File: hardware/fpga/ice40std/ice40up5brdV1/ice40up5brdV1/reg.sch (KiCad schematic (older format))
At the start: 1 part

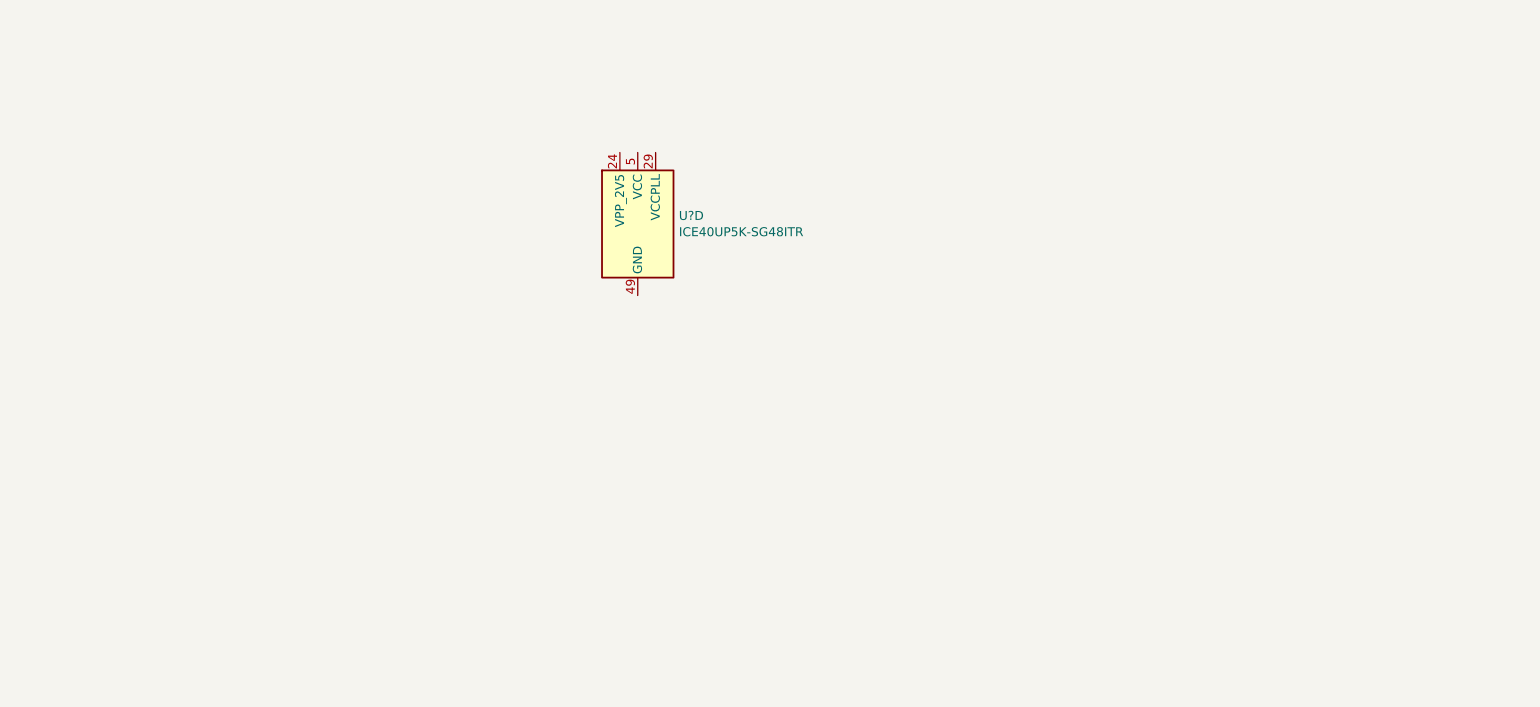
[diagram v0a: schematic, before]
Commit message: usb => mcu => ice40 fpga => NAND flash bridge started
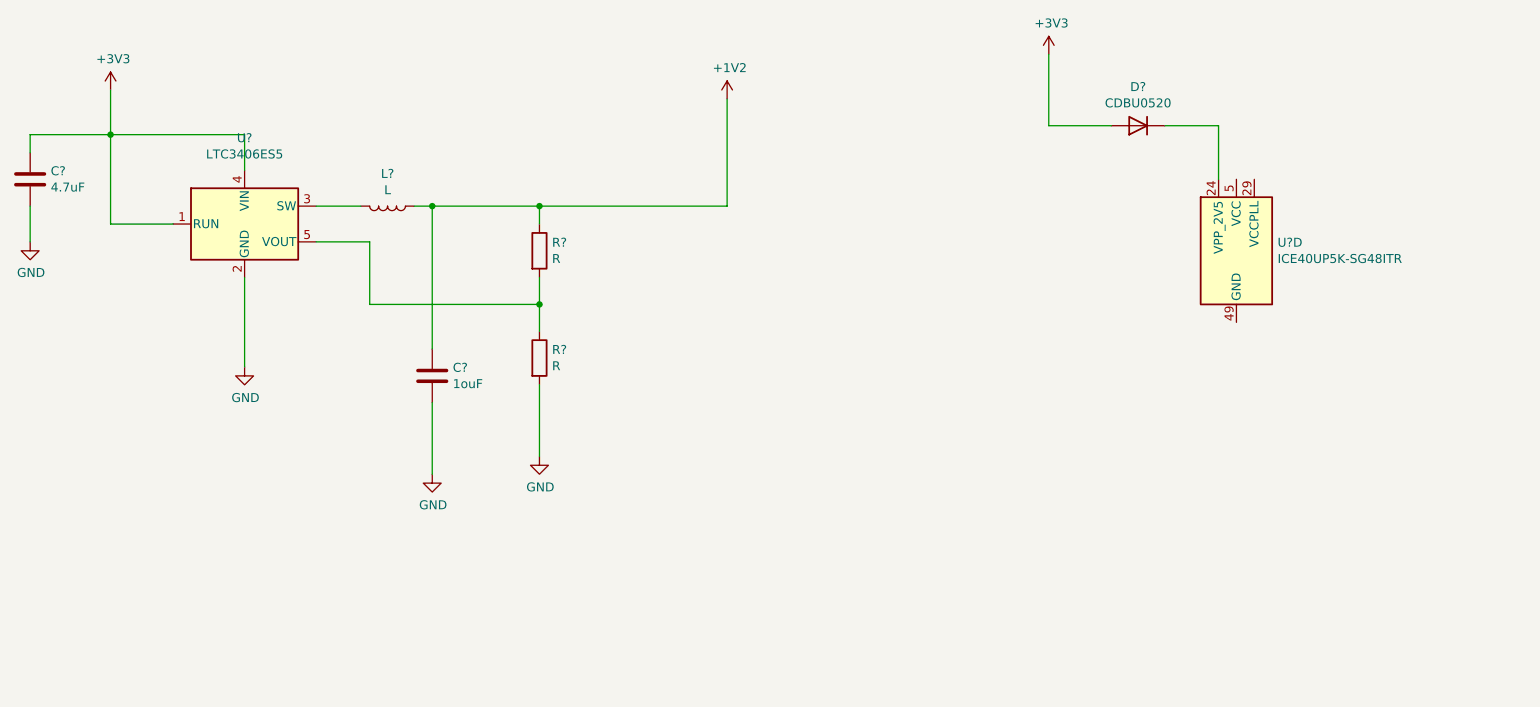
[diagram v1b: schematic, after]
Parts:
- added C?: 4.7uF, Capacitor_SMD:C_0402_1005Metric, symbol Device:C
- added C?: 1ouF, Capacitor_SMD:C_0603_1608Metric, symbol Device:C
- added D?: CDBU0520, Diode_SMD:D_0603_1608Metric, symbol Device:D
- added L?: L, symbol Device:L
- added R? (x2): R, symbol Device:R
- added U?: LTC3406ES5, Package_TO_SOT_SMD:TSOT-23-5, symbol Regulator_Switching:LTC3406ES5
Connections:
- net at U?.24 (VPP_2V5): now also D?.1 (K)
- new net: L?.2, U?.3 (SW)
- new net: R?.1, R?.2, U?.5 (VOUT)
- new net +1V2: C?.1, L?.1, R?.1
- new net +3V3: C?.1, D?.2 (A), U?.1 (RUN), U?.4 (VIN)
- new net GND: C?.2, C?.2, R?.2, U?.2 (GND)
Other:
- moved on the sheet: U?D
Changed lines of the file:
@@
 L FPGA_Lattice:ICE40UP5K-SG48ITR U?
 U 4 1 60A7161F
-P 4500 3100
-F 0 "U?" H 4730 3146 50  0000 L CNN
-F 1 "ICE40UP5K-SG48ITR" H 4730 3055 50  0000 L CNN
-F 2 "Package_DFN_QFN:QFN-48-1EP_7x7mm_P0.5mm_EP5.6x5.6mm" H 4500 1750 50  0001 C CNN
-F 3 "http://www.latticesemi.com/Products/FPGAandCPLD/iCE40Ultra" H 4100 4100 50  0001 C CNN
-	4    4500 3100
-	1    0    0    -1
-$EndComp
+P 7850 3250
+F 0 "U?" H 8080 3296 50  0000 L CNN
+F 1 "ICE40UP5K-SG48ITR" H 8080 3205 50  0000 L CNN
+F 2 "Package_DFN_QFN:QFN-48-1EP_7x7mm_P0.5mm_EP5.6x5.6mm" H 7850 1900 50  0001 C CNN
+F 3 "http://www.latticesemi.com/Products/FPGAandCPLD/iCE40Ultra" H 7450 4250 50  0001 C CNN
+	4    7850 3250
+	1    0    0    -1
+$EndComp
+$Comp
+L Regulator_Switching:LTC3406ES5 U?
+U 1 1 60A7BA3D
+P 2300 3100
+F 0 "U?" H 2300 3581 50  0000 C CNN
+F 1 "LTC3406ES5" H 2300 3490 50  0000 C CNN
+F 2 "Package_TO_SOT_SMD:TSOT-23-5" H 3000 2850 50  0001 C CNN
+F 3 "https://www.analog.com/media/en/technical-documentation/data-sheets/3406b12fs.pdf" H 2300 3050 50  0001 C CNN
+	1    2300 3100
+	1    0    0    -1
+$EndComp
+$Comp
+L Device:D D?
+U 1 1 60A801A2
+P 7300 2550
+F 0 "D?" H 7300 2333 50  0000 C CNN
+F 1 "CDBU0520" H 7300 2424 50  0000 C CNN
+F 2 "Diode_SMD:D_0603_1608Metric" H 7300 2550 50  0001 C CNN
+F 3 "~" H 7300 2550 50  0001 C CNN
+	1    7300 2550
+	-1   0    0    1
+$EndComp
+$Comp
+L Device:L L?
+U 1 1 60A846BB
+P 3100 3000
+F 0 "L?" V 2919 3000 50  0000 C CNN
+F 1 "L" V 3010 3000 50  0000 C CNN
+F 2 "" H 3100 3000 50  0001 C CNN
+F 3 "~" H 3100 3000 50  0001 C CNN
+	1    3100 3000
+	0    1    1    0
+$EndComp
+$Comp
+L Device:R R?
+U 1 1 60A869B1
+P 3950 3250
+F 0 "R?" H 4020 3296 50  0000 L CNN
+F 1 "R" H 4020 3205 50  0000 L CNN
+F 2 "" V 3880 3250 50  0001 C CNN
+F 3 "~" H 3950 3250 50  0001 C CNN
+	1    3950 3250
+	1    0    0    -1
+$EndComp
+$Comp
+L Device:R R?
+U 1 1 60A86DB5
+P 3950 3850
+F 0 "R?" H 4020 3896 50  0000 L CNN
+F 1 "R" H 4020 3805 50  0000 L CNN
+F 2 "" V 3880 3850 50  0001 C CNN
+F 3 "~" H 3950 3850 50  0001 C CNN
+	1    3950 3850
+	1    0    0    -1
+$EndComp
+$Comp
+L power:GND #PWR?
+U 1 1 60A872CB
+P 3950 4400
+F 0 "#PWR?" H 3950 4150 50  0001 C CNN
+F 1 "GND" H 3955 4227 50  0000 C CNN
+F 2 "" H 3950 4400 50  0001 C CNN
+F 3 "" H 3950 4400 50  0001 C CNN
+	1    3950 4400
+	1    0    0    -1
+$EndComp
+Wire Wire Line
+	3950 4000 3950 4400
+Wire Wire Line
+	3950 3700 3950 3550
+Wire Wire Line
+	3250 3000 3350 3000
+Wire Wire Line
+	3950 3000 3950 3100
+Wire Wire Line
+	2700 3000 2950 3000
+Wire Wire Line
+	2700 3200 3000 3200
+Wire Wire Line
+	3000 3200 3000 3550
+Wire Wire Line
+	3000 3550 3950 3550
+Connection ~ 3950 3550
+Wire Wire Line
+	3950 3550 3950 3400
+$Comp
+L power:GND #PWR?
+U 1 1 60A8868D
+P 2300 3900
+F 0 "#PWR?" H 2300 3650 50  0001 C CNN
+F 1 "GND" H 2305 3727 50  0000 C CNN
+F 2 "" H 2300 3900 50  0001 C CNN
+F 3 "" H 2300 3900 50  0001 C CNN
+	1    2300 3900
+	1    0    0    -1
+$EndComp
+Wire Wire Line
+	2300 3400 2300 3900
+$Comp
+L power:+3V3 #PWR?
+U 1 1 60A899B6
+P 1550 2350
+F 0 "#PWR?" H 1550 2200 50  0001 C CNN
+F 1 "+3V3" H 1565 2523 50  0000 C CNN
+F 2 "" H 1550 2350 50  0001 C CNN
+F 3 "" H 1550 2350 50  0001 C CNN
+	1    1550 2350
+	1    0    0    -1
+$EndComp
+Wire Wire Line
+	1550 2350 1550 2600
+Wire Wire Line
+	1550 3100 1900 3100
+Wire Wire Line
+	2300 2800 2300 2600
+Wire Wire Line
+	2300 2600 1550 2600
+Connection ~ 1550 2600
+Wire Wire Line
+	1550 2600 1550 3100
+$Comp
+L Device:C C?
+U 1 1 60A8A29C
+P 1100 2850
+F 0 "C?" H 1215 2896 50  0000 L CNN
+F 1 "4.7uF" H 1215 2805 50  0000 L CNN
+F 2 "Capacitor_SMD:C_0402_1005Metric" H 1138 2700 50  0001 C CNN
+F 3 "~" H 1100 2850 50  0001 C CNN
+	1    1100 2850
+	1    0    0    -1
+$EndComp
+Wire Wire Line
+	1100 2700 1100 2600
+Wire Wire Line
+	1100 2600 1550 2600
+$Comp
+L power:GND #PWR?
+U 1 1 60A8AD40
+P 1100 3200
+F 0 "#PWR?" H 1100 2950 50  0001 C CNN
+F 1 "GND" H 1105 3027 50  0000 C CNN
+F 2 "" H 1100 3200 50  0001 C CNN
+F 3 "" H 1100 3200 50  0001 C CNN
+	1    1100 3200
+	1    0    0    -1
+$EndComp
+Wire Wire Line
+	1100 3000 1100 3200
+$Comp
+L Device:C C?
+U 1 1 60A8B955
+P 3350 3950
+F 0 "C?" H 3465 3996 50  0000 L CNN
+F 1 "1ouF" H 3465 3905 50  0000 L CNN
+F 2 "Capacitor_SMD:C_0603_1608Metric" H 3388 3800 50  0001 C CNN
+F 3 "~" H 3350 3950 50  0001 C CNN
+	1    3350 3950
+	1    0    0    -1
+$EndComp
+Wire Wire Line
+	3350 3000 3350 3800
+Connection ~ 3350 3000
+Wire Wire Line
+	3350 3000 3950 3000
+$Comp
+L power:GND #PWR?
+U 1 1 60A8CBDB
+P 3350 4500
+F 0 "#PWR?" H 3350 4250 50  0001 C CNN
+F 1 "GND" H 3355 4327 50  0000 C CNN
+F 2 "" H 3350 4500 50  0001 C CNN
+F 3 "" H 3350 4500 50  0001 C CNN
+	1    3350 4500
+	1    0    0    -1
+$EndComp
+Wire Wire Line
+	3350 4100 3350 4500
+$Comp
+L power:+1V2 #PWR?
+U 1 1 60A8DB44
+P 5000 2400
+F 0 "#PWR?" H 5000 2250 50  0001 C CNN
+F 1 "+1V2" H 5015 2573 50  0000 C CNN
+F 2 "" H 5000 2400 50  0001 C CNN
+F 3 "" H 5000 2400 50  0001 C CNN
+	1    5000 2400
+	1    0    0    -1
+$EndComp
+Wire Wire Line
+	3950 3000 5000 3000
+Wire Wire Line
+	5000 3000 5000 2400
+Connection ~ 3950 3000
+Wire Wire Line
+	7450 2550 7750 2550
+Wire Wire Line
+	7750 2550 7750 2850
+$Comp
+L power:+3V3 #PWR?
+U 1 1 60A9198E
+P 6800 2150
+F 0 "#PWR?" H 6800 2000 50  0001 C CNN
+F 1 "+3V3" H 6815 2323 50  0000 C CNN
+F 2 "" H 6800 2150 50  0001 C CNN
+F 3 "" H 6800 2150 50  0001 C CNN
+	1    6800 2150
+	1    0    0    -1
+$EndComp
+Wire Wire Line
+	6800 2150 6800 2550
+Wire Wire Line
+	6800 2550 7150 2550
 $EndSCHEMATC

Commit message: usb => mcu => ice40 fpga => NAND flash bridge started
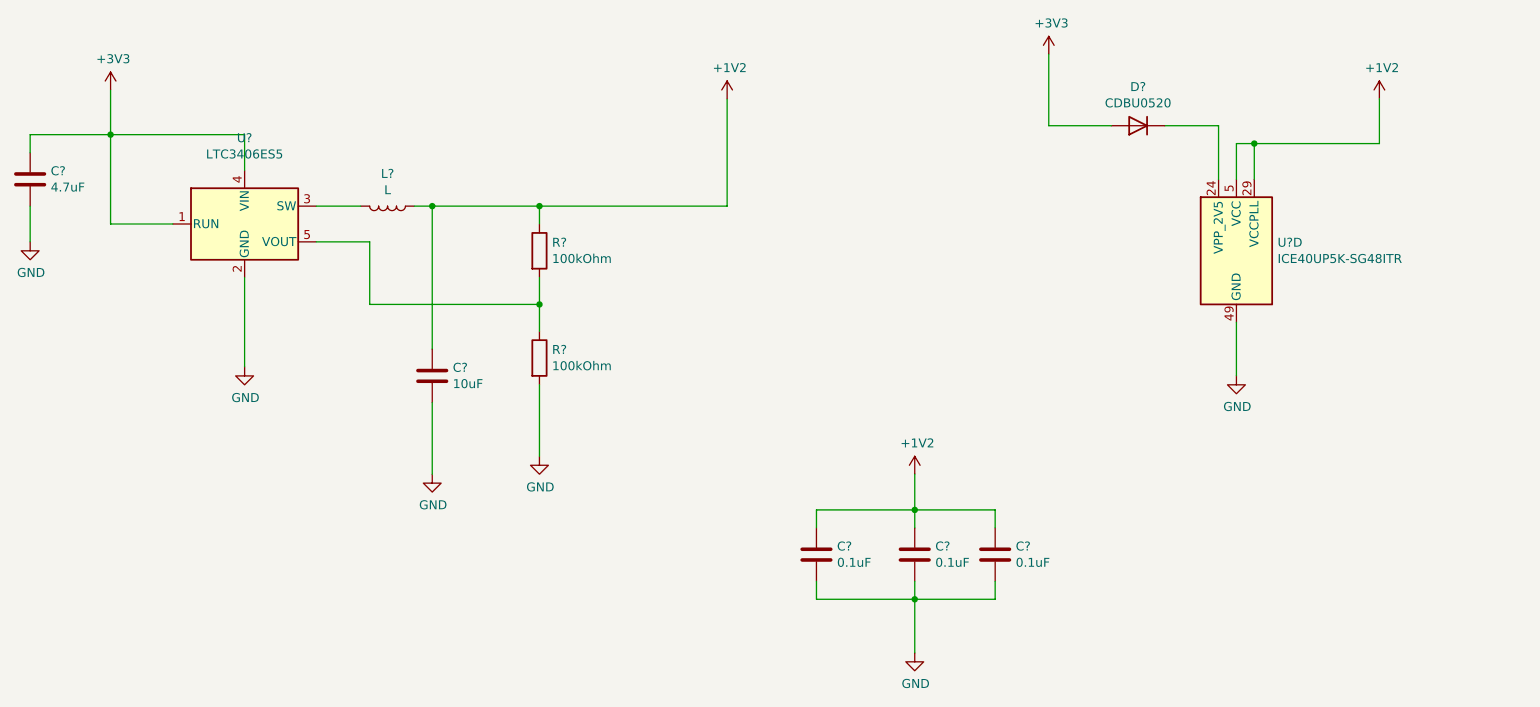
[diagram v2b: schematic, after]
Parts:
- added C? (x3): 0.1uF, Capacitor_SMD:C_0402_1005Metric, symbol Device:C
- C?: value 1ouF -> 10uF
- L?: footprint (none) -> Inductor_SMD:L_1210_3225Metric
- R? (x2): value R -> 100kOhm; footprint (none) -> Resistor_SMD:R_0402_1005Metric
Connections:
- net +1V2: now also U?.29 (VCCPLL), U?.30 (VCC), U?.5 (VCC), C?.1, C?.1, C?.1
- net GND: now also U?.49 (GND), C?.2, C?.2, C?.2
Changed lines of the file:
@@
 F 0 "L?" V 2919 3000 50  0000 C CNN
 F 1 "L" V 3010 3000 50  0000 C CNN
-F 2 "" H 3100 3000 50  0001 C CNN
+F 2 "Inductor_SMD:L_1210_3225Metric" H 3100 3000 50  0001 C CNN
 F 3 "~" H 3100 3000 50  0001 C CNN
 	1    3100 3000
@@
 P 3950 3250
 F 0 "R?" H 4020 3296 50  0000 L CNN
-F 1 "R" H 4020 3205 50  0000 L CNN
-F 2 "" V 3880 3250 50  0001 C CNN
+F 1 "100kOhm" H 4020 3205 50  0000 L CNN
+F 2 "Resistor_SMD:R_0402_1005Metric" V 3880 3250 50  0001 C CNN
 F 3 "~" H 3950 3250 50  0001 C CNN
 	1    3950 3250
@@
 P 3950 3850
 F 0 "R?" H 4020 3896 50  0000 L CNN
-F 1 "R" H 4020 3805 50  0000 L CNN
-F 2 "" V 3880 3850 50  0001 C CNN
+F 1 "100kOhm" H 4020 3805 50  0000 L CNN
+F 2 "Resistor_SMD:R_0402_1005Metric" V 3880 3850 50  0001 C CNN
 F 3 "~" H 3950 3850 50  0001 C CNN
 	1    3950 3850
@@
 P 3350 3950
 F 0 "C?" H 3465 3996 50  0000 L CNN
-F 1 "1ouF" H 3465 3905 50  0000 L CNN
+F 1 "10uF" H 3465 3905 50  0000 L CNN
 F 2 "Capacitor_SMD:C_0603_1608Metric" H 3388 3800 50  0001 C CNN
 F 3 "~" H 3350 3950 50  0001 C CNN
@@
 Wire Wire Line
 	6800 2550 7150 2550
+$Comp
+L power:+1V2 #PWR?
+U 1 1 60A94F17
+P 8650 2400
+F 0 "#PWR?" H 8650 2250 50  0001 C CNN
+F 1 "+1V2" H 8665 2573 50  0000 C CNN
+F 2 "" H 8650 2400 50  0001 C CNN
+F 3 "" H 8650 2400 50  0001 C CNN
+	1    8650 2400
+	1    0    0    -1
+$EndComp
+Wire Wire Line
+	7850 2850 7850 2650
+Wire Wire Line
+	7850 2650 7950 2650
+Wire Wire Line
+	8650 2650 8650 2400
+Wire Wire Line
+	7950 2850 7950 2650
+Connection ~ 7950 2650
+Wire Wire Line
+	7950 2650 8650 2650
+$Comp
+L power:+1V2 #PWR?
+U 1 1 60A96F10
+P 6050 4500
+F 0 "#PWR?" H 6050 4350 50  0001 C CNN
+F 1 "+1V2" H 6065 4673 50  0000 C CNN
+F 2 "" H 6050 4500 50  0001 C CNN
+F 3 "" H 6050 4500 50  0001 C CNN
+	1    6050 4500
+	1    0    0    -1
+$EndComp
+$Comp
+L Device:C C?
+U 1 1 60A9752A
+P 5500 4950
+F 0 "C?" H 5615 4996 50  0000 L CNN
+F 1 "0.1uF" H 5615 4905 50  0000 L CNN
+F 2 "Capacitor_SMD:C_0402_1005Metric" H 5538 4800 50  0001 C CNN
+F 3 "~" H 5500 4950 50  0001 C CNN
+	1    5500 4950
+	1    0    0    -1
+$EndComp
+$Comp
+L Device:C C?
+U 1 1 60A97958
+P 6500 4950
+F 0 "C?" H 6615 4996 50  0000 L CNN
+F 1 "0.1uF" H 6615 4905 50  0000 L CNN
+F 2 "Capacitor_SMD:C_0402_1005Metric" H 6538 4800 50  0001 C CNN
+F 3 "~" H 6500 4950 50  0001 C CNN
+	1    6500 4950
+	1    0    0    -1
+$EndComp
+Wire Wire Line
+	5500 4800 5500 4700
+Wire Wire Line
+	5500 4700 6050 4700
+Wire Wire Line
+	6500 4700 6500 4800
+Wire Wire Line
+	6050 4500 6050 4700
+Wire Wire Line
+	5500 5100 5500 5200
+Wire Wire Line
+	5500 5200 6050 5200
+Wire Wire Line
+	6500 5200 6500 5100
+$Comp
+L power:GND #PWR?
+U 1 1 60A9A1A4
+P 7850 3950
+F 0 "#PWR?" H 7850 3700 50  0001 C CNN
+F 1 "GND" H 7855 3777 50  0000 C CNN
+F 2 "" H 7850 3950 50  0001 C CNN
+F 3 "" H 7850 3950 50  0001 C CNN
+	1    7850 3950
+	1    0    0    -1
+$EndComp
+$Comp
+L power:GND #PWR?
+U 1 1 60A9A678
+P 6050 5500
+F 0 "#PWR?" H 6050 5250 50  0001 C CNN
+F 1 "GND" H 6055 5327 50  0000 C CNN
+F 2 "" H 6050 5500 50  0001 C CNN
+F 3 "" H 6050 5500 50  0001 C CNN
+	1    6050 5500
+	1    0    0    -1
+$EndComp
+Wire Wire Line
+	6050 5200 6050 5500
+Connection ~ 6050 5200
+Wire Wire Line
+	6050 5200 6500 5200
+Wire Wire Line
+	7850 3650 7850 3950
+$Comp
+L Device:C C?
+U 1 1 60A9DB64
+P 6050 4950
+F 0 "C?" H 6165 4996 50  0000 L CNN
+F 1 "0.1uF" H 6165 4905 50  0000 L CNN
+F 2 "Capacitor_SMD:C_0402_1005Metric" H 6088 4800 50  0001 C CNN
+F 3 "~" H 6050 4950 50  0001 C CNN
+	1    6050 4950
+	1    0    0    -1
+$EndComp
+Connection ~ 6050 4700
+Wire Wire Line
+	6050 4700 6500 4700
+Wire Wire Line
+	6050 5200 6050 5100
+Wire Wire Line
+	6050 4800 6050 4700
 $EndSCHEMATC
